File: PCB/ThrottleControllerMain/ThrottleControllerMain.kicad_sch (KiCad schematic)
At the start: 39 parts, among them J1 Conn_ARM_JTAG_SWD_10, J2 Conn_01x02, J4 Conn_01x04_Pin, J5 Screw_Terminal_01x02, J6 Screw_Terminal_01x02, P1 USB_C_Plug, U1 RP2040, U2 TLV493D, U3 NCP1117-3.3_SOT223, U5 W25Q32JVSS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

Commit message: PCB footprint layout is mostly complete.
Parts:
- removed J1: Conn_ARM_JTAG_SWD_10, Connector_PinHeader_2.54mm:PinHeader_2x05_P2.54mm_Vertical, symbol Connector:Conn_ARM_JTAG_SWD_10
- removed J5, J6: Screw_Terminal_01x02, TerminalBlock_Phoenix:TerminalBlock_Phoenix_MPT-0,5-2-2.54_1x02_P2.54mm_Horizontal, symbol Connector:Screw_Terminal_01x02
- added H1, H2, H3, H4: MountingHole, MountingHole:MountingHole_3.2mm_M3, symbol Mechanical:MountingHole
- added J1: Conn_01x03_Socket, Connector_JST:JST_SH_BM03B-SRSS-TB_1x03-1MP_P1.00mm_Vertical, symbol Connector:Conn_01x03_Socket
- added J3, J5: Conn_01x02_Socket, Connector_JST:JST_SH_BM02B-SRSS-TB_1x02-1MP_P1.00mm_Vertical, symbol Connector:Conn_01x02_Socket
- Y1: footprint Crystal:Crystal_SMD_5032-2Pin_5.0x3.2mm -> Crystal:Crystal_SMD_3225-4Pin_3.2x2.5mm
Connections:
- net GND: now also J1.1 (Pin_1), J3.2 (Pin_2), J5.2 (Pin_2)
- net at R9.2: now also J3.1 (Pin_1)
- net at U1.24 (SWCLK): now also J1.3 (Pin_3)
- net at U1.25 (SWD): now also J1.2 (Pin_2)
- net at R10.2: now also J5.1 (Pin_1)

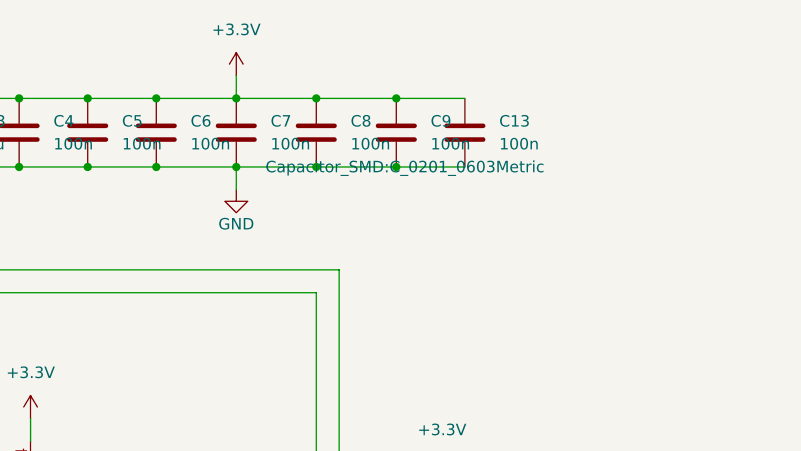
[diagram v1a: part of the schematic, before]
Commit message: PCB positioning improvements
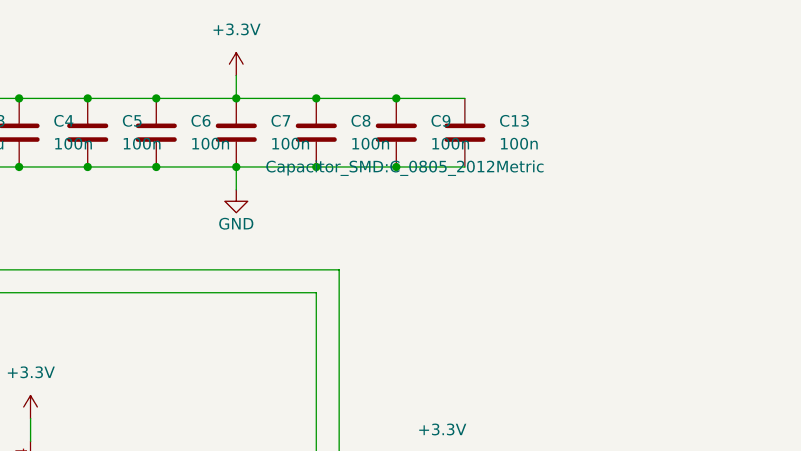
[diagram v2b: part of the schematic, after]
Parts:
- C13, C5, C6, C7, C8, C9: footprint Capacitor_SMD:C_0201_0603Metric -> Capacitor_SMD:C_0805_2012Metric
- C4: footprint Capacitor_SMD:C_0603_1608Metric -> Capacitor_SMD:C_0805_2012Metric
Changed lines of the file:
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@@
       (effects (font (size 1.27 1.27)) (justify left))
     )
-    (property "Footprint" "Capacitor_SMD:C_0201_0603Metric" (at 221.9452 33.02 0)
+    (property "Footprint" "Capacitor_SMD:C_0805_2012Metric" (at 221.9452 33.02 0)
       (effects (font (size 1.27 1.27)) hide)
     )
@@
       (effects (font (size 1.27 1.27)) (justify left))
     )
-    (property "Footprint" "Capacitor_SMD:C_0201_0603Metric" (at 213.0552 33.02 0)
+    (property "Footprint" "Capacitor_SMD:C_0805_2012Metric" (at 213.0552 33.02 0)
       (effects (font (size 1.27 1.27)) hide)
     )
@@
       (effects (font (size 1.27 1.27)) (justify left))
     )
-    (property "Footprint" "Capacitor_SMD:C_0201_0603Metric" (at 239.7252 33.02 0)
+    (property "Footprint" "Capacitor_SMD:C_0805_2012Metric" (at 239.7252 33.02 0)
       (effects (font (size 1.27 1.27)))
     )
@@
       (effects (font (size 1.27 1.27)) (justify left))
     )
-    (property "Footprint" "Capacitor_SMD:C_0201_0603Metric" (at 205.4352 33.02 0)
+    (property "Footprint" "Capacitor_SMD:C_0805_2012Metric" (at 205.4352 33.02 0)
       (effects (font (size 1.27 1.27)) hide)
     )
@@
       (effects (font (size 1.27 1.27)) (justify left))
     )
-    (property "Footprint" "Capacitor_SMD:C_0201_0603Metric" (at 230.8352 33.02 0)
+    (property "Footprint" "Capacitor_SMD:C_0805_2012Metric" (at 230.8352 33.02 0)
       (effects (font (size 1.27 1.27)) hide)
     )
@@
       (effects (font (size 1.27 1.27)) (justify left))
     )
-    (property "Footprint" "Capacitor_SMD:C_0603_1608Metric" (at 197.8152 33.02 0)
+    (property "Footprint" "Capacitor_SMD:C_0805_2012Metric" (at 197.8152 33.02 0)
       (effects (font (size 1.27 1.27)) hide)
     )
@@
       (effects (font (size 1.27 1.27)) (justify left))
     )
-    (property "Footprint" "Capacitor_SMD:C_0201_0603Metric" (at 247.3452 33.02 0)
-      (effects (font (size 1.27 1.27)) hide)
-    )
+    (property "Footprint" "Capacitor_SMD:C_0805_2012Metric" (at 247.3452 33.02 0)
+      (effects (font (size 1.27 1.27)) hide)
+    )

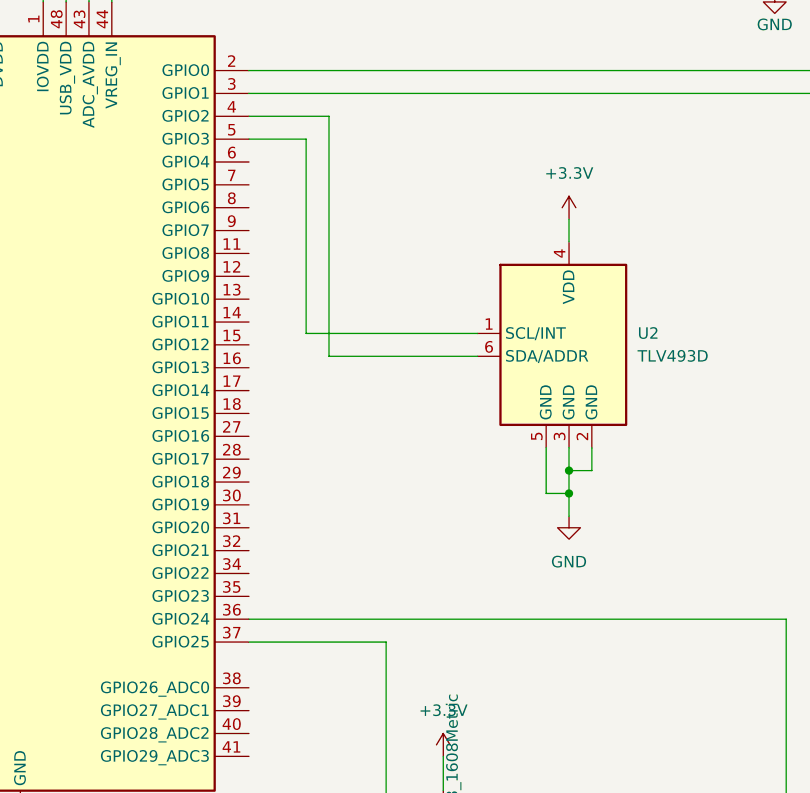
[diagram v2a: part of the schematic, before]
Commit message: Added serial-port debug header.
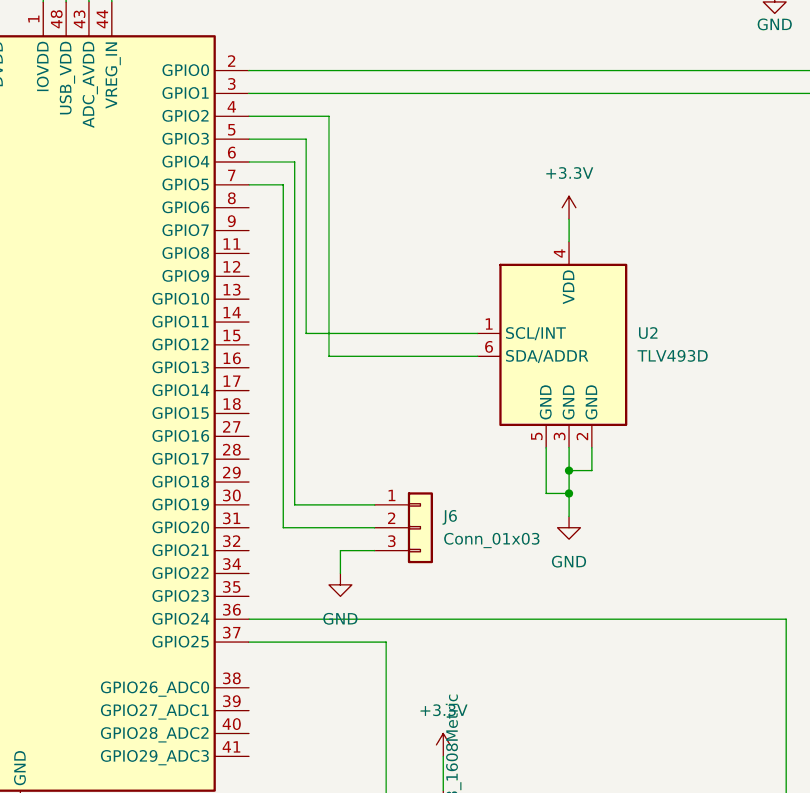
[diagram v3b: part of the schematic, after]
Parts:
- added J6: Conn_01x03, Connector_PinHeader_2.54mm:PinHeader_1x03_P2.54mm_Vertical, symbol Connector_Generic:Conn_01x03
- J4: footprint Connector_JST:JST_SH_SM04B-SRSS-TB_1x04-1MP_P1.00mm_Horizontal -> Connector_JST:JST_SH_BM04B-SRSS-TB_1x04-1MP_P1.00mm_Vertical
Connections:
- net GND: now also J6.3 (Pin_3)
- net at U1.6 (GPIO4): now also J6.1 (Pin_1)
- net at U1.7 (GPIO5): now also J6.2 (Pin_2)
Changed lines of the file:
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@@
+    (stroke (width 0) (type default))
+  )
+  (wire (pts (xy 167.64 92.71) (xy 167.64 54.61))
     (stroke (width 0) (type default))
   )
@@
     (stroke (width 0) (type default))
   )
+  (wire (pts (xy 176.53 97.79) (xy 172.72 97.79))
+    (stroke (width 0) (type default))
+  )
   (wire (pts (xy 229.87 33.02) (xy 238.76 33.02))
     (stroke (width 0) (type default))
@@
     (stroke (width 0) (type default))
   )
+  (wire (pts (xy 172.72 97.79) (xy 172.72 100.33))
+    (stroke (width 0) (type default))
+  )
+  (wire (pts (xy 167.64 54.61) (xy 162.56 54.61))
+    (stroke (width 0) (type default))
+  )
   (wire (pts (xy 111.76 130.81) (xy 137.16 130.81))
     (stroke (width 0) (type default))
@@
     (stroke (width 0) (type default))
   )
+  (wire (pts (xy 166.37 57.15) (xy 162.56 57.15))
+    (stroke (width 0) (type default))
+  )
   (wire (pts (xy 222.25 137.16) (xy 233.68 137.16))
     (stroke (width 0) (type default))
@@
     (stroke (width 0) (type default))
   )
+  (wire (pts (xy 166.37 95.25) (xy 166.37 57.15))
+    (stroke (width 0) (type default))
+  )
   (wire (pts (xy 60.96 172.72) (xy 68.58 172.72))
     (stroke (width 0) (type default))
@@
     (stroke (width 0) (type default))
   )
+  (wire (pts (xy 176.53 95.25) (xy 166.37 95.25))
+    (stroke (width 0) (type default))
+  )
   (wire (pts (xy 101.6 74.93) (xy 111.76 74.93))
     (stroke (width 0) (type default))
   )
   (wire (pts (xy 60.96 170.18) (xy 68.58 170.18))
+    (stroke (width 0) (type default))
+  )
+  (wire (pts (xy 176.53 92.71) (xy 167.64 92.71))
     (stroke (width 0) (type default))
   )
@@
         (path "/3c5ca945-e315-4685-b8c2-2aea1653922a"
           (reference "#PWR024") (unit 1)
+        )
+      )
+    )
+  )
+  (symbol (lib_id "Connector_Generic:Conn_01x03") (at 181.61 95.25 0) (unit 1)
+    (in_bom yes) (on_board yes) (dnp no) (fields_autoplaced)
+    (property "Reference" "J6" (at 184.15 93.98 0)
+      (effects (font (size 1.27 1.27)) (justify left))
+    )
+    (property "Value" "Conn_01x03" (at 184.15 96.52 0)
+      (effects (font (size 1.27 1.27)) (justify left))
+    )
+    (property "Footprint" "Connector_PinHeader_2.54mm:PinHeader_1x03_P2.54mm_Vertical" (at 181.61 95.25 0)
+      (effects (font (size 1.27 1.27)) hide)
+    )
+    (property "Datasheet" "~" (at 181.61 95.25 0)
+      (effects (font (size 1.27 1.27)) hide)
+    )
+    (pin "1")
+    (pin "2")
+    (pin "3")
+    (instances
+      (project "ThrottleControllerMain"
+        (path "/3c5ca945-e315-4685-b8c2-2aea1653922a"
+          (reference "J6") (unit 1)
         )
       )
@@
     )
   )
+  (symbol (lib_id "power:GND") (at 172.72 100.33 0) (unit 1)
+    (in_bom yes) (on_board yes) (dnp no) (fields_autoplaced)
+    (property "Reference" "#PWR030" (at 172.72 106.68 0)
+      (effects (font (size 1.27 1.27)) hide)
+    )
+    (property "Value" "GND" (at 172.72 105.41 0)
+      (effects (font (size 1.27 1.27)))
+    )
+    (property "Footprint" "" (at 172.72 100.33 0)
+      (effects (font (size 1.27 1.27)) hide)
+    )
+    (property "Datasheet" "" (at 172.72 100.33 0)
+      (effects (font (size 1.27 1.27)) hide)
+    )
+    (pin "1")
+    (instances
+      (project "ThrottleControllerMain"
+        (path "/3c5ca945-e315-4685-b8c2-2aea1653922a"
+          (reference "#PWR030") (unit 1)
+        )
+      )
+    )
+  )
   (symbol (lib_id "power:GND") (at 83.82 156.21 0) (unit 1)
     (in_bom yes) (on_board yes) (dnp no) (fields_autoplaced)
@@
       (effects (font (size 1.27 1.27)) (justify right))
     )
-    (property "Footprint" "Connector_JST:JST_SH_SM04B-SRSS-TB_1x04-1MP_P1.00mm_Horizontal" (at 252.73 78.74 0)
-      (effects (font (size 1.27 1.27)) hide)
-    )
+    (property "Footprint" "Connector_JST:JST_SH_BM04B-SRSS-TB_1x04-1MP_P1.00mm_Vertical" (at 252.73 78.74 0)
+      (effects (font (size 1.27 1.27)) hide)
+    )

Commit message: Finished first draft of routing.
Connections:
- net QSPI_SCLK: now also U5.6 (CLK)
- net QSPI_SD1: now also U5.2 (DO(IO1))
- net QSPI_SD2: now also U5.3 (IO2)
- net QSPI_SD3: now also U5.7 (IO3)
- net QSPI_SDO: now also U5.5 (DI(IO0))
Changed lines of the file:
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@@
-    (stroke (width 0) (type default))
-  )
-  (wire (pts (xy 60.96 177.8) (xy 68.58 177.8))
     (stroke (width 0) (type default))
   )
@@
     (stroke (width 0) (type default))
   )
-  (wire (pts (xy 60.96 175.26) (xy 68.58 175.26))
-    (stroke (width 0) (type default))
-  )
   (wire (pts (xy 196.85 140.97) (xy 201.93 140.97))
     (stroke (width 0) (type default))
@@
     (stroke (width 0) (type default))
   )
+  (wire (pts (xy 58.42 172.72) (xy 68.58 172.72))
+    (stroke (width 0) (type default))
+  )
   (wire (pts (xy 250.19 143.51) (xy 254 143.51))
     (stroke (width 0) (type default))
@@
     (stroke (width 0) (type default))
   )
+  (wire (pts (xy 58.42 177.8) (xy 68.58 177.8))
+    (stroke (width 0) (type default))
+  )
   (wire (pts (xy 132.08 26.67) (xy 132.08 29.21))
     (stroke (width 0) (type default))
@@
     (stroke (width 0) (type default))
   )
-  (wire (pts (xy 60.96 167.64) (xy 68.58 167.64))
-    (stroke (width 0) (type default))
-  )
   (wire (pts (xy 196.85 25.4) (xy 204.47 25.4))
     (stroke (width 0) (type default))
@@
     (stroke (width 0) (type default))
   )
+  (wire (pts (xy 58.42 170.18) (xy 68.58 170.18))
+    (stroke (width 0) (type default))
+  )
   (wire (pts (xy 151.13 163.83) (xy 151.13 168.91))
     (stroke (width 0) (type default))
@@
     (stroke (width 0) (type default))
   )
+  (wire (pts (xy 58.42 167.64) (xy 68.58 167.64))
+    (stroke (width 0) (type default))
+  )
   (wire (pts (xy 187.96 76.2) (xy 171.45 76.2))
     (stroke (width 0) (type default))
@@
     (stroke (width 0) (type default))
   )
+  (wire (pts (xy 58.42 175.26) (xy 68.58 175.26))
+    (stroke (width 0) (type default))
+  )
   (wire (pts (xy 116.84 163.83) (xy 116.84 161.29))
     (stroke (width 0) (type default))
@@
     (stroke (width 0) (type default))
   )
-  (wire (pts (xy 60.96 172.72) (xy 68.58 172.72))
-    (stroke (width 0) (type default))
-  )
   (wire (pts (xy 60.96 110.49) (xy 111.76 110.49))
     (stroke (width 0) (type default))
@@
     (stroke (width 0) (type default))
   )
-  (wire (pts (xy 60.96 170.18) (xy 68.58 170.18))
-    (stroke (width 0) (type default))
-  )

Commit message: Small edits to schematic
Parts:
- R5: value 1k -> 10k
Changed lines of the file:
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@@
   (junction (at 137.16 130.81) (diameter 0) (color 0 0 0 0)
   )
-  (junction (at 77.47 44.45) (diameter 0) (color 0 0 0 0)
-  )
   (junction (at 238.76 33.02) (diameter 0) (color 0 0 0 0)
   )
@@
     (stroke (width 0) (type default))
   )
-  (wire (pts (xy 72.39 44.45) (xy 77.47 44.45))
-    (stroke (width 0) (type default))
-  )
   (wire (pts (xy 101.6 72.39) (xy 111.76 72.39))
     (stroke (width 0) (type default))
@@
   )
   (wire (pts (xy 68.58 52.07) (xy 111.76 52.07))
-    (stroke (width 0) (type default))
-  )
-  (wire (pts (xy 72.39 105.41) (xy 72.39 44.45))
     (stroke (width 0) (type default))
   )
@@
       (effects (font (size 1.27 1.27)) (justify left))
     )
-    (property "Value" "1k" (at 80.01 30.48 0)
-      (effects (font (size 1.27 1.27)) (justify left))
-    )
+    (property "Value" "10k" (at 80.01 30.48 0)
+      (effects (font (size 1.27 1.27)) (justify left))
+    )
